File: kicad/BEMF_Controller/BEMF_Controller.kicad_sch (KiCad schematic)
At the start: 100 parts, among them J1 HEADER4VALULOK, J2 HEADER6, J3 FUSE, J4 Coil_A, J5 Coil_B, J6 Coil_C, J7 Vin, Q1 C3M0280090D, Q2 C3M0280090D, Q3 C3M0280090D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

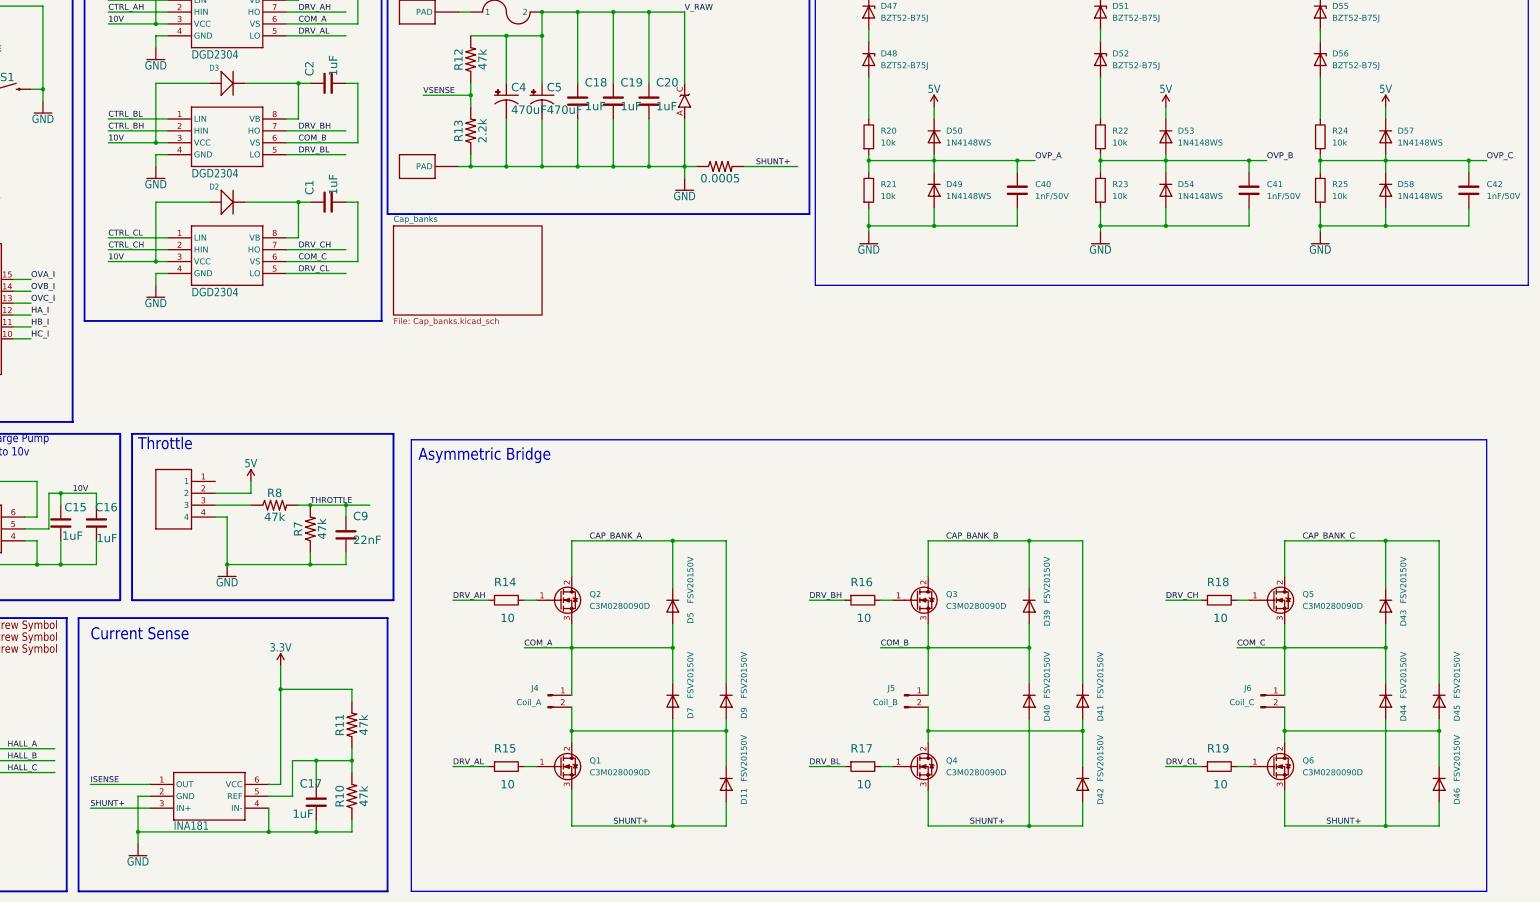
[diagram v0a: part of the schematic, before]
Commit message: Added buffers for analog inputs
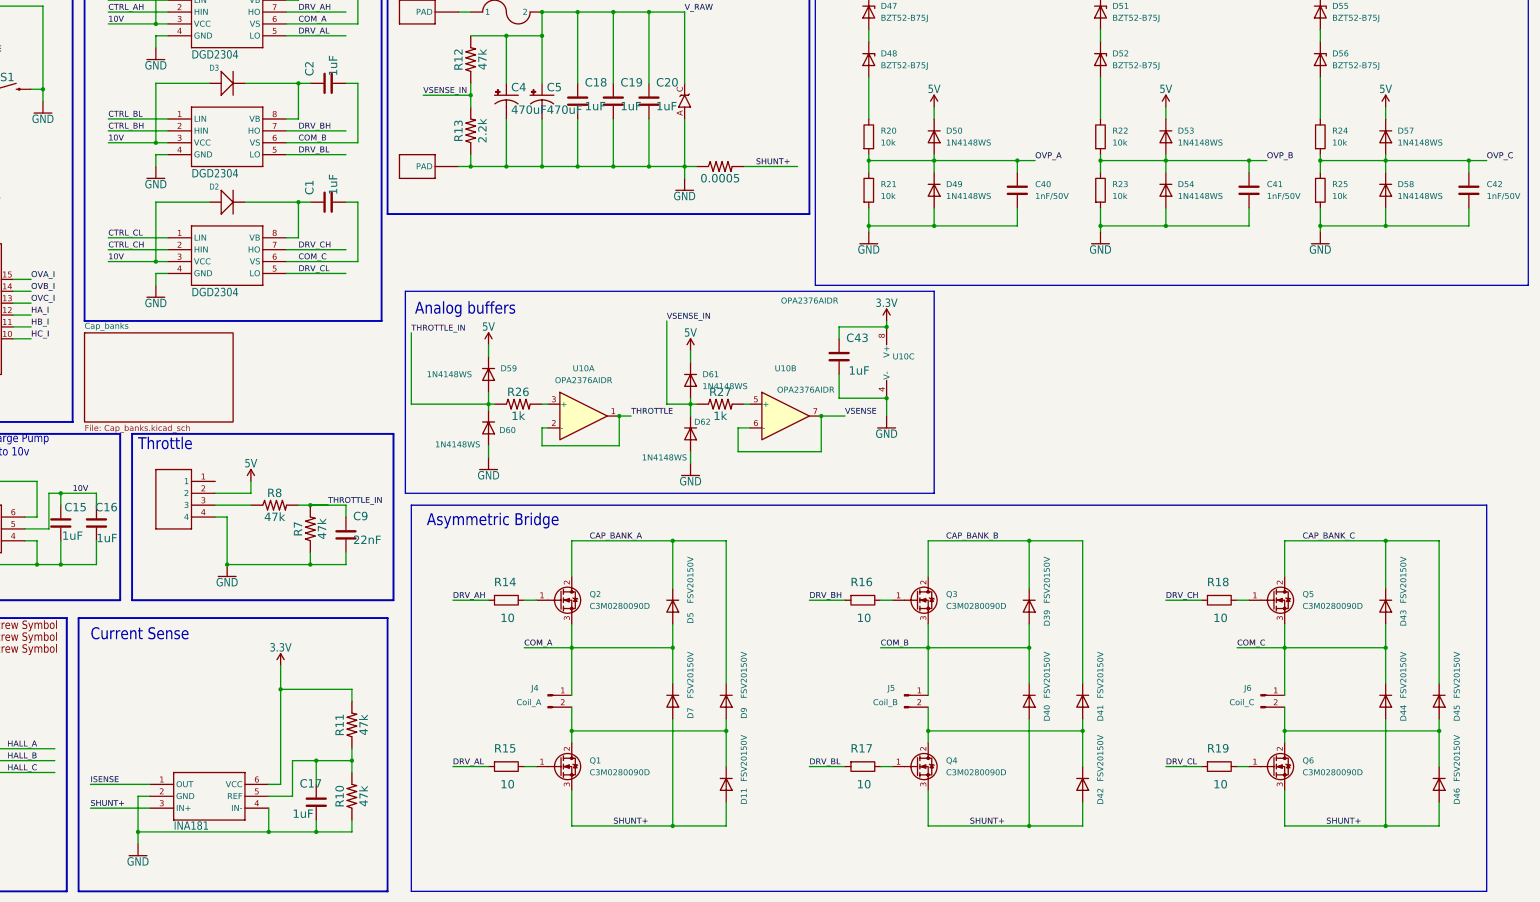
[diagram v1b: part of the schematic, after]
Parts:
- added C43: 1uF, Capacitor_SMD:C_1812_4532Metric, symbol Component_Library:CHV1812N250105MXT
- added D59, D60, D61, D62: 1N4148WS, Diode_SMD:D_SOD-323, symbol Diode:1N4148WS
- added R26, R27: 1k, main:1206, symbol main-eagle-import:RESISTOR1206
- added U10: OPA2376AIDR, Package_SO:SOIC-8-1EP_3.9x4.9mm_P1.27mm_EP2.29x3mm, symbol Component_Library:OPA2376AIDR
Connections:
- net 3.3V: now also C43.1, U10.8 (V+)
- net 5V: now also D59.1 (K), D61.1 (K)
- net GND: now also C43.2, D60.2 (A), D62.2 (A), U10.4 (V-)
- net THROTTLE: now also U10.1, U10.2 (-); no longer C9.1, R7.2, R8.2
- net VSENSE: now also U10.6 (-), U10.7; no longer R12.1, R13.2
- new net: R27.2, U10.5 (+)
- new net: R26.2, U10.3 (+)
- new net THROTTLE_IN: C9.1, D59.2 (A), D60.1 (K), R26.1, R7.2, R8.2
- new net VSENSE_IN: D61.2 (A), D62.1 (K), R12.1, R13.2, R27.1
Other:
- note added: "Analog buffers"

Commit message: Added few more decoupling capacitors.
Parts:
- added C44, C45, C46: 1uF, Capacitor_SMD:C_1812_4532Metric, symbol Component_Library:CHV1812N250105MXT
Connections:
- net 3.3V: now also C44.1, C45.1, C46.1
- net GND: now also C44.2, C45.2, C46.2

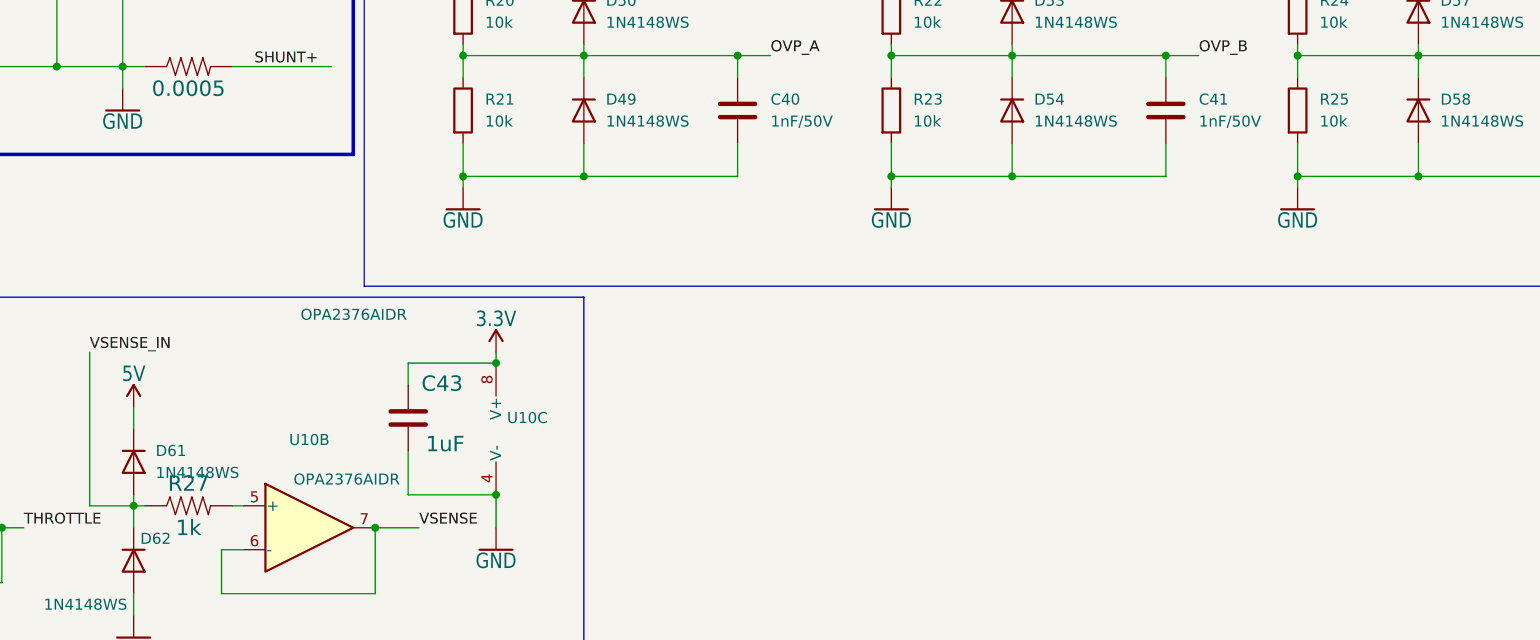
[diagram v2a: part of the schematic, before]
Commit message: Referenced ovp circuit to v_shunt+ rather than ground.
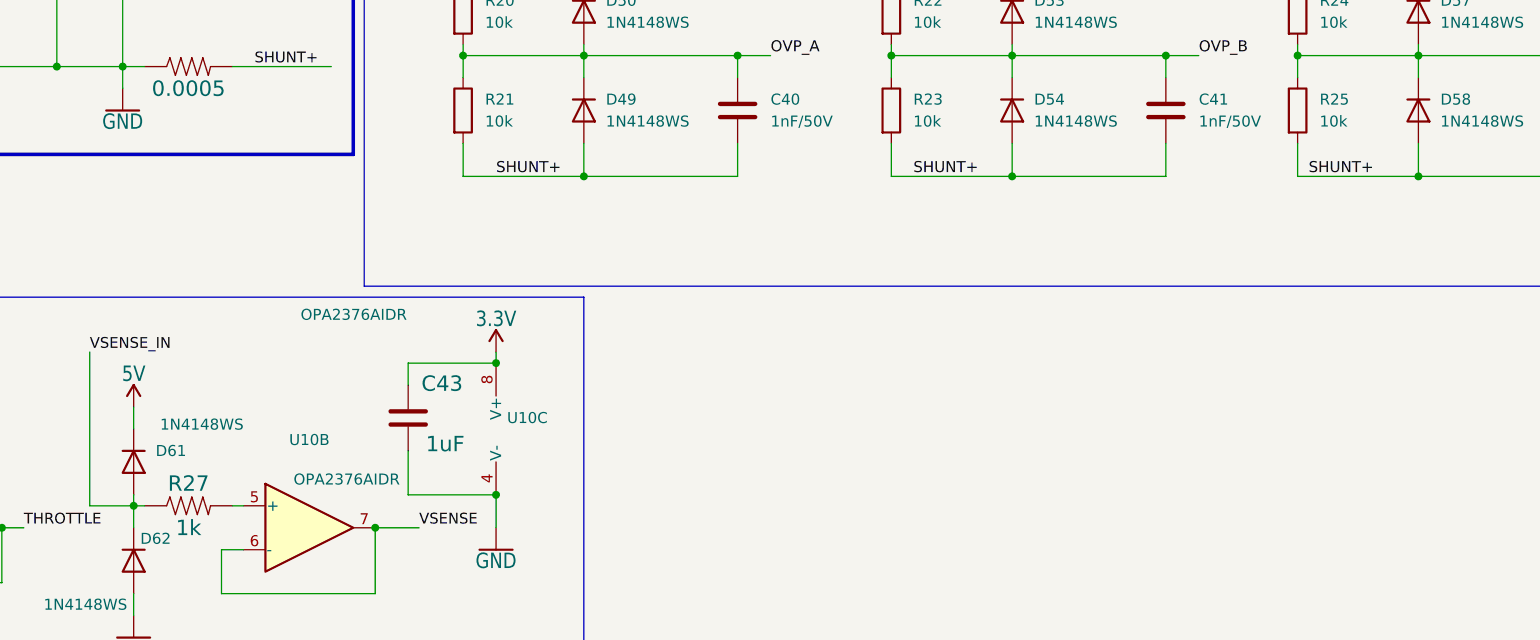
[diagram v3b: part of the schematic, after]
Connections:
- net GND: no longer C40.2, C41.2, C42.2, D49.2 (A), D54.2 (A), D58.2 (A), R21.2, R23.2, R25.2
- net SHUNT+: now also C40.2, C41.2, C42.2, D49.2 (A), D54.2 (A), D58.2 (A), R21.2, R23.2, R25.2

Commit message: Added external spi ADC for current and voltage sense per bridge
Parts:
- removed C17, C43, C46: 1uF, Capacitor_SMD:C_1812_4532Metric, symbol Component_Library:CHV1812N250105MXT
- removed C40, C41, C42: 1nF/50V, Capacitor_SMD:C_1210_3225Metric, symbol Device:C
- removed D47, D48, D51, D52, D55, D56: BZT52-B75J, Diode_SMD:D_SOD-123F, symbol Component_Library:BZT52-B75J
- removed D49, D50, D53, D54, D57, D58, D59, D60, D61, D62: 1N4148WS, Diode_SMD:D_SOD-323, symbol Diode:1N4148WS
- removed R10, R11: 47k, main:1206, symbol main-eagle-import:RESISTOR1206
- removed R20, R21, R22, R23, R24, R25: 10k, Resistor_SMD:R_1210_3225Metric, symbol Device:R
- removed R26, R27: 1k, main:1206, symbol main-eagle-import:RESISTOR1206
- removed R9: 0.0005, main:R2512, symbol main-eagle-import:RESISTOR
- removed U10: OPA2376AIDR, Package_SO:SOIC-8-1EP_3.9x4.9mm_P1.27mm_EP2.29x3mm, symbol Component_Library:OPA2376AIDR
- removed U2: INA181, main:SOT23-6, symbol main-eagle-import:INA181
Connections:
- net THROTTLE_IN is gone; now on net THROTTLE: C9.1, R7.2, R8.2
- net SPI0_TX: now reaches U1.5 (GP3), U1.P$5 (GP3)
- net SPI0_RX: now reaches U1.6 (GP4), U1.P$6 (GP4)
- net SPI0_CSn: now reaches U1.7 (GP5), U1.P$7 (GP5)
- net OVA_I: no longer names the net of U1.1 (GP0), U1.P$1 (GP0)
- net OVA_I: no longer U9.15 (OUTA)
- net OVB_I: no longer names the net of U1.2 (GP1), U1.P$2 (GP1)
- net OVB_I: no longer U9.14 (OUTB)
- net OVC_I renamed SPI0_SCK
- net SPI0_SCK: no longer U9.13 (OUTC)
- net OVP_A: no longer names the net of U9.2 (INA)
- net OVP_B: no longer names the net of U9.3 (INB)
- net OVP_C: no longer names the net of U9.4 (INC)
- removed net SHUNT+: D11.3 (K), D40.3 (K), D42.3 (K), D44.3 (K), D46.3 (K), D7.3 (K), Q1.3 (S), Q4.3 (S), Q6.3 (S)
- new net SHUNT_A+: D11.3 (K), D7.3 (K), Q1.3 (S)
- new net SHUNT_B+: D40.3 (K), D42.3 (K), Q4.3 (S)
- new net SHUNT_C+: D44.3 (K), D46.3 (K), Q6.3 (S)
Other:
- added sheet Analog_IO (Analog_IO.kicad_sch)
- added sheet Current_sense (Current_sense.kicad_sch)
- note removed: "Analog buffers"
- note removed: "Current Sense"
- note removed: "Overvoltage Detection"

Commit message: Several updates to analog section
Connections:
- net CAP_BANK_A renamed CAP_BANK_A+
- net CAP_BANK_B renamed CAP_BANK_B+
- net CAP_BANK_C renamed CAP_BANK_C+
- net SHUNT_A+ renamed CAP_BANK_A-
- net SHUNT_B+ renamed CAP_BANK_B-
- net SHUNT_C+ renamed CAP_BANK_C-

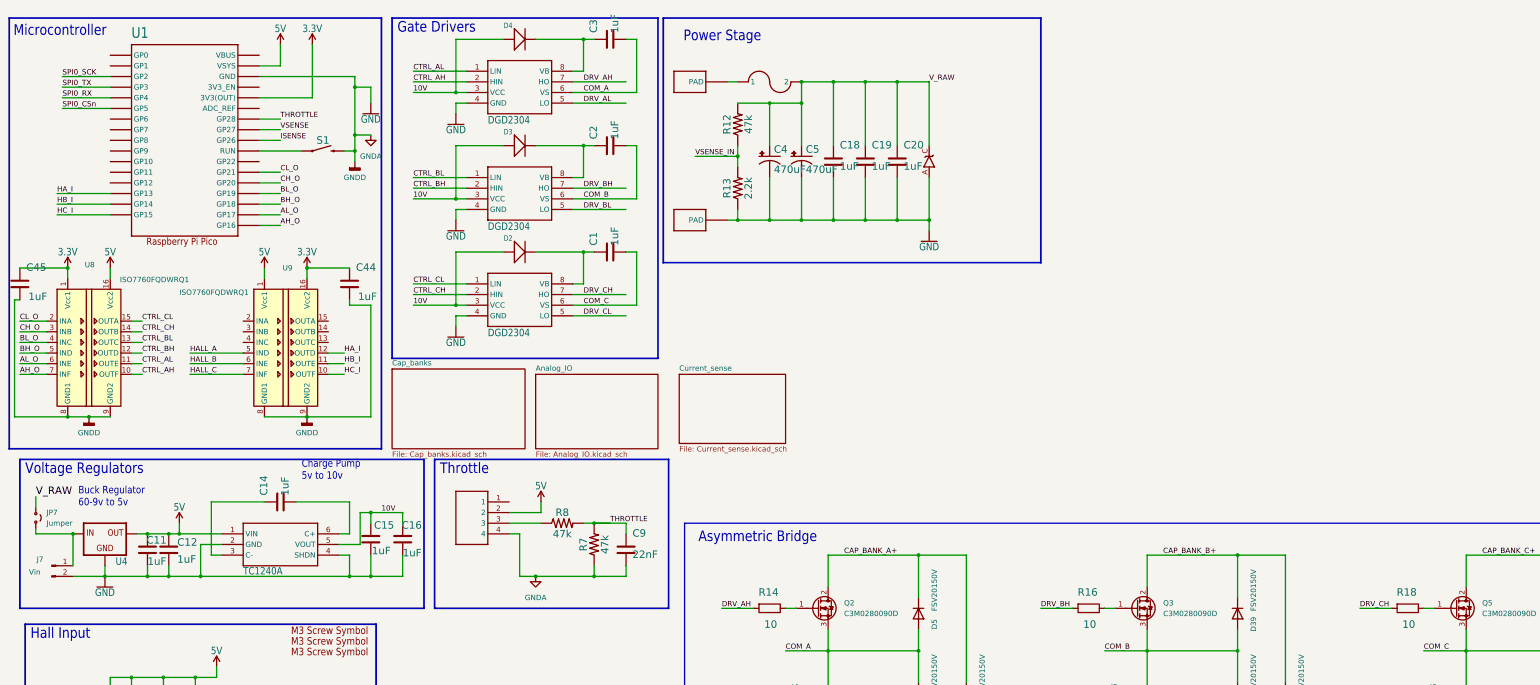
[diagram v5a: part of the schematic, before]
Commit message: Further work on a/o current sensing circuits.
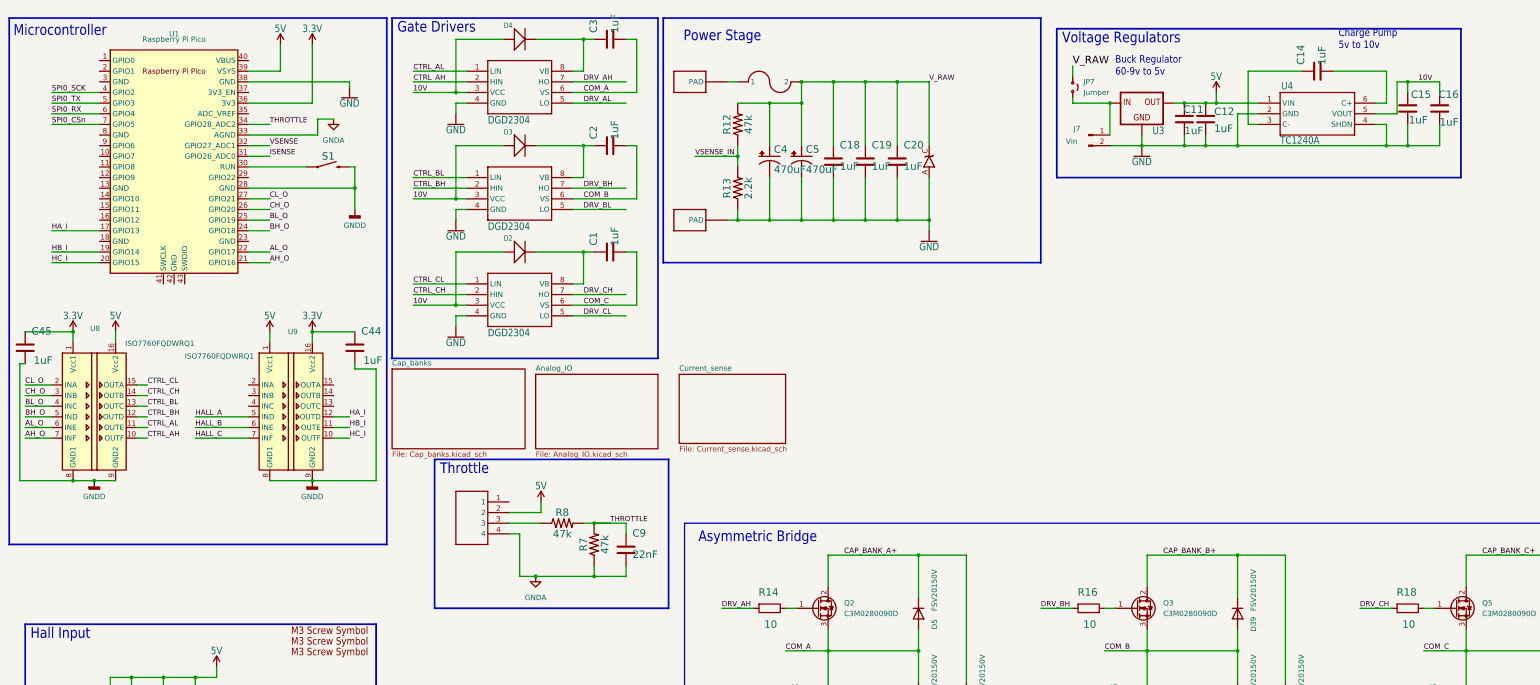
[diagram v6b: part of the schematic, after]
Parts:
- removed U1: RASPBERRY_PICO-NO_DEBUG, main:PICO-PKG-NO_DEBUG, symbol main-eagle-import:RASPBERRY_PICO-NO_DEBUG
- removed U3: TC1240A, main:SOT23-6, symbol main-eagle-import:TC1240A
- removed U4: V_REG_78XX, main:V78W_BACKWARDS, symbol main-eagle-import:V_REG_78XX
- added U1: Raspberry Pi Pico, footprints:RPi_Pico_SMD_TH, symbol Component_Library:Raspberry Pi Pico
- added U3: V_REG_78XX, main:V78W_BACKWARDS, symbol main-eagle-import:V_REG_78XX
- added U4: TC1240A, main:SOT23-6, symbol main-eagle-import:TC1240A
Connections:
- net 10V: now also U4.5 (VOUT)
- net 3.3V: now also U1.36 (3V3)
- net 5V: now also U1.39 (VSYS), U3.OUT, U4.1 (VIN)
- net AH_O: now also U1.21 (GPIO16)
- net AL_O: now also U1.22 (GPIO17)
- net BH_O: now also U1.24 (GPIO18)
- net BL_O: now also U1.25 (GPIO19)
- net CH_O: now also U1.26 (GPIO20)
- net CL_O: now also U1.27 (GPIO21)
- net GND: now also U1.38 (GND), U3.GND, U4.2 (GND), U4.4 (SHDN); no longer C44.2, C45.2, C9.2, J1.4, J2.1, R7.1, S1.3 (2), U8.8 (GND1), U8.9 (GND2), U9.8 (GND1), U9.9 (GND2)
- net HA_I: now also U1.17 (GPIO13)
- net HB_I: now also U1.19 (GPIO14)
- net HC_I: now also U1.20 (GPIO15)
- net ISENSE: now also U1.31 (GPIO26_ADC0)
- net SPI0_CSn: now also U1.7 (GPIO5)
- net SPI0_RX: now also U1.6 (GPIO4)
- net SPI0_SCK: now also U1.4 (GPIO2)
- net SPI0_TX: now also U1.5 (GPIO3)
- net THROTTLE: now also U1.34 (GPIO28_ADC2)
- net VSENSE: now also U1.32 (GPIO27_ADC1)
- net at J7.1 (Pin_1), JP7.2 (B): now also U3.IN
- net at S1.1: now also U1.30 (RUN)
- net at C14.1: now also U4.3 (C-)
- net at C14.2: now also U4.6 (C+)
- new net GNDA: C9.2, J1.4, R7.1, U1.33 (AGND)
- new net GNDD: C44.2, C45.2, J2.1, S1.3 (2), U1.28 (GND), U8.8 (GND1), U8.9 (GND2), U9.8 (GND1), U9.9 (GND2)
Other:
- moved on the sheet: C44, C45, S1, U8, U9
